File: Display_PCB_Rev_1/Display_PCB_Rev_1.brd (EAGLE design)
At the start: 5 parts, among them J1 71430-015

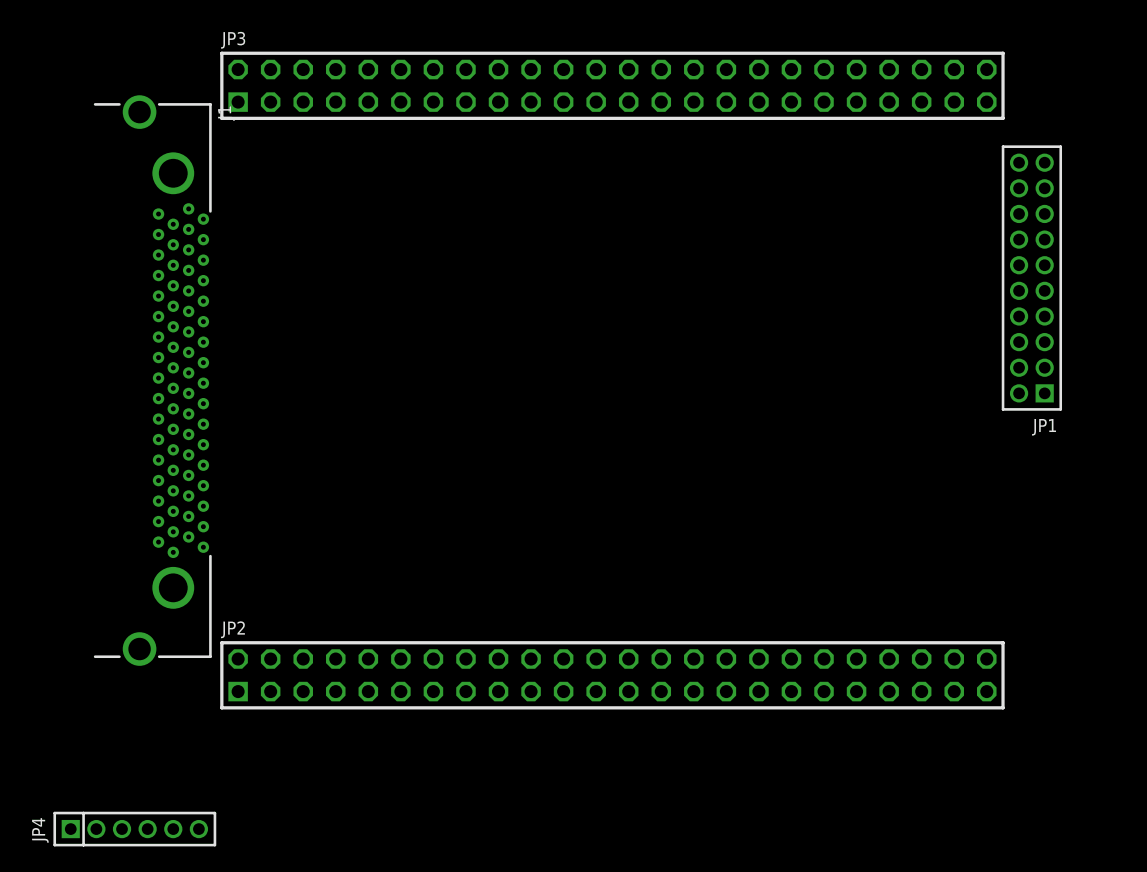
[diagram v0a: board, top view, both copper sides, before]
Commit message: Cleaned up schematic and layout; Added DC Barrel Jack and coupling capacitor; filtering circuit for shield
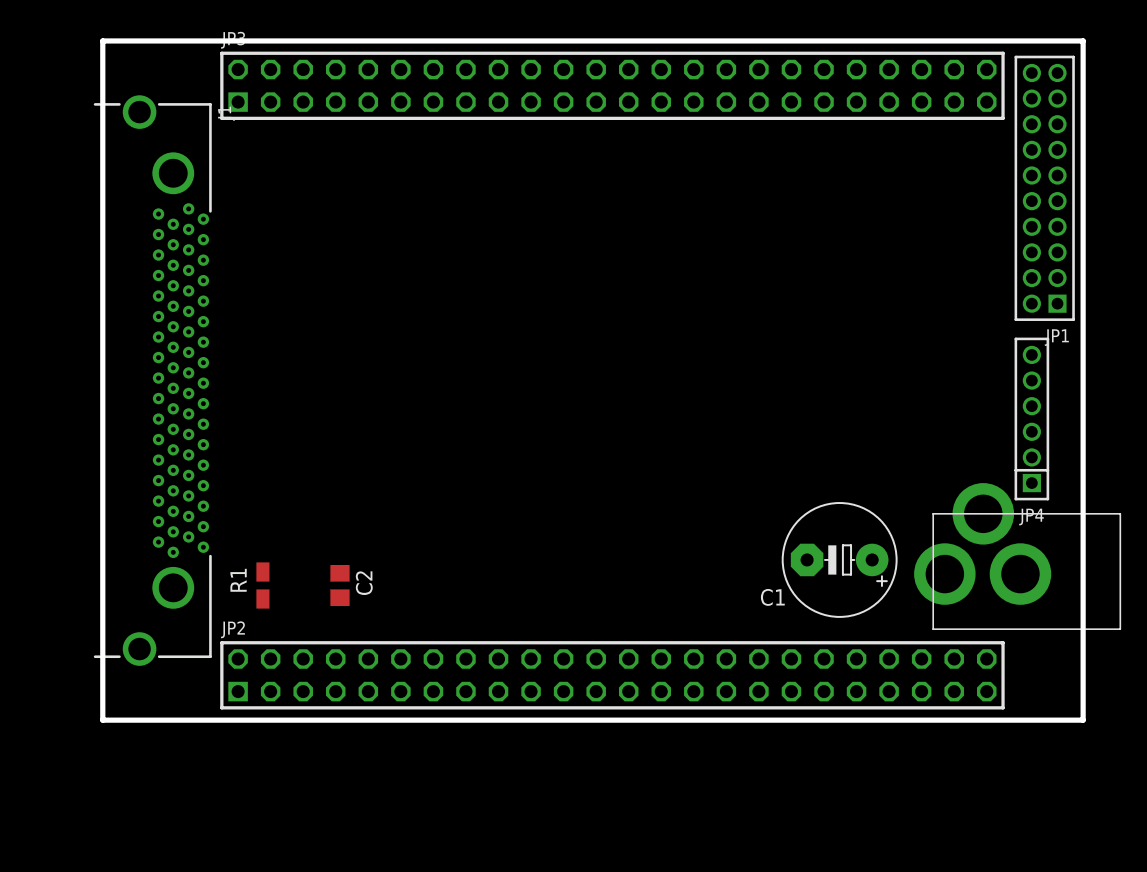
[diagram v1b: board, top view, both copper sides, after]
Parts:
- added C1: 220u, resistor:E5-8,5
- added C2: 1n, resistor:C0805
- added R1: 1M, resistor:R0805W
- added U$1: 2.1MMJACKTHM, adafruit:PJ-102A
- moved JP4 77.0 mm to (85.0, 51.0), turned to 90 degrees
- moved JP1 7.07 mm to (86.0, 69.0)
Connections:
- removed net N$2: JP3.25, JP3.41
- removed net N$4: J1.41
- new net DE: JP4.4
- new net VCC_12: C1.+, JP4.5, JP4.6, U$1.TIP
- net GND: now also C1.-, C2.2, JP2.1, JP2.11, JP2.12, JP2.17, JP2.2, JP2.26, JP2.33, JP2.42, JP3.16, JP3.23, JP3.32, JP3.39, JP3.48, JP3.7, JP4.1, JP4.2, R1.1, U$1.RING, U$1.RING_SW; no longer JP1.4, JP2.16, JP2.23, JP2.32, JP2.39, JP2.48, JP2.7, JP3.1, JP3.11, JP3.12, JP3.17, JP3.2, JP3.26, JP3.33, JP3.42
- net N$1: now also C2.1, R1.2; no longer JP3.18, JP3.34
- net VCC: now also J1.19, JP2.18, JP2.25, JP2.34, JP2.41, JP3.15, JP3.24, JP3.31, JP3.40, JP3.8; no longer JP1.3
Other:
- board outline added: 76.5 x 53 mm

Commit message: Added .gitignore; removed unnecessary files; added routes for VCC, GND, and VCC_12
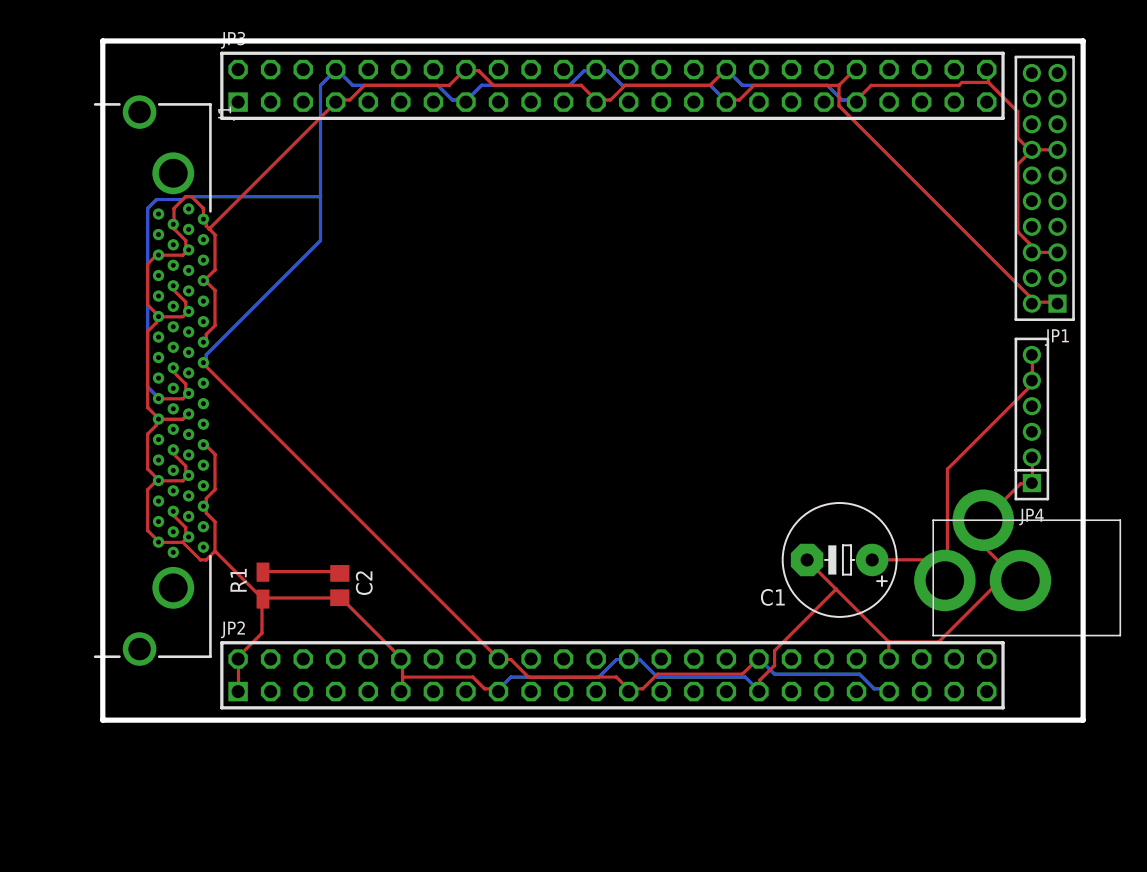
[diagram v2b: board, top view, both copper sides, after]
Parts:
- moved U$1 0.50 mm to (87.5, 38.5)
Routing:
- net GND: track 0.00 -> 274.4 mm
- net VCC: track 0.00 -> 198.1 mm
- net VCC_12: track 0.00 -> 28.1 mm
- net N$1: track 0.00 -> 6.06 mm

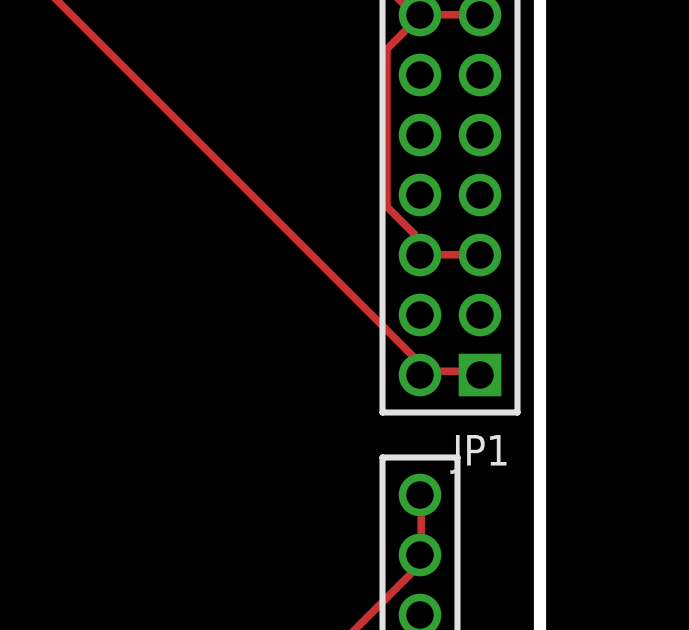
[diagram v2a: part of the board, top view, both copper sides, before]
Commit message: first set of differential pairs
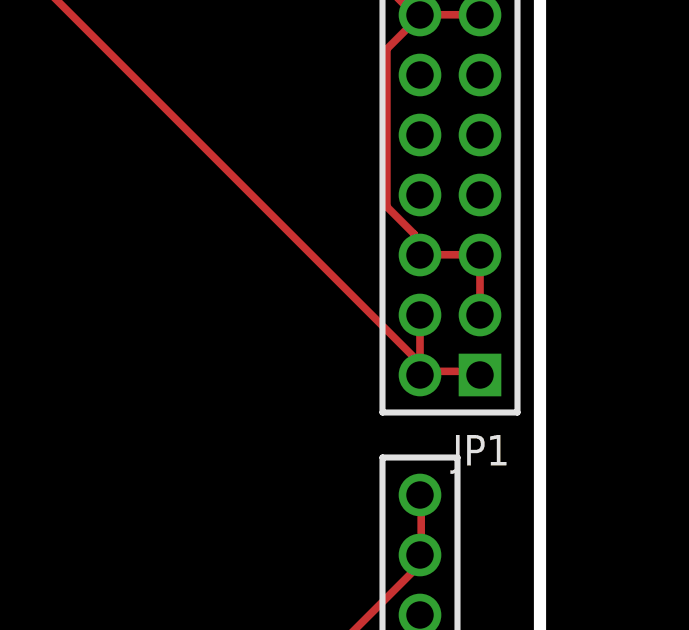
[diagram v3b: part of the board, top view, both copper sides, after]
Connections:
- net CLK_N: now also J1.66, JP3.12; no longer J1.9
- net CLK_P: now also J1.32, JP3.11; no longer J1.10
- net DE: now also J1.3, JP2.30
- net GND: now also JP1.3
- net RXIN0_N: now also J1.41, JP3.2; no longer J1.31
- net RXIN0_P: now also J1.7, JP3.1; no longer J1.32
- net RXIN1_N: now also J1.47, JP3.4; no longer J1.25
- net RXIN1_P: now also J1.13, JP3.3; no longer J1.26
- net RXIN2_N: now also J1.60, JP3.10; no longer J1.17
- net RXIN2_P: now also J1.26, JP3.9; no longer J1.18
- net VCC: now also JP1.4
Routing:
- net VCC: track 198.1 -> 200.1 mm
- net GND: track 274.4 -> 276.4 mm
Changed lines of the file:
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@@
 <wire x1="20.8026" y1="65.8368" x2="30.6324" y2="75.6666" width="0.254" layer="1"/>
 <wire x1="30.6324" y1="75.6666" x2="30.68" y2="75.73" width="0.254" layer="1"/>
-<wire x1="16.6878" y1="58.5216" x2="18" y2="56.595" width="0" layer="19" extent="1-1"/>
+<contactref element="JP1" pad="3"/>
+<wire x1="18" y1="56.595" x2="16.6878" y2="58.5216" width="0" layer="19" extent="1-1"/>
+<wire x1="87" y1="64" x2="87" y2="62" width="0.254" layer="1"/>
 </signal>
 <signal name="VCC">
@@
 <wire x1="50.9778" y1="78.1812" x2="51" y2="78.27" width="0.254" layer="16"/>
 <wire x1="40.9194" y1="75.8952" x2="40.84" y2="75.73" width="0.254" layer="16"/>
+<contactref element="JP1" pad="4"/>
+<wire x1="85" y1="62" x2="85" y2="60" width="0.254" layer="1"/>
 </signal>
 <signal name="RXIN0_N">
 <contactref element="JP1" pad="7"/>
-<contactref element="J1" pad="31"/>
-<wire x1="20.35" y1="64.995" x2="87" y2="66" width="0" layer="19" extent="1-1"/>
+<contactref element="J1" pad="41"/>
+<contactref element="JP3" pad="2"/>
+<wire x1="23.06" y1="78.27" x2="87" y2="66" width="0" layer="19" extent="1-1"/>
+<wire x1="18" y1="45.395" x2="23.06" y2="78.27" width="0" layer="19" extent="1-1"/>
 </signal>
 <signal name="RXIN1_N">
 <contactref element="JP1" pad="9"/>
-<contactref element="J1" pad="25"/>
-<wire x1="20.35" y1="60.195" x2="87" y2="68" width="0" layer="19" extent="1-1"/>
+<contactref element="J1" pad="47"/>
+<contactref element="JP3" pad="4"/>
+<wire x1="25.6" y1="78.27" x2="87" y2="68" width="0" layer="19" extent="1-1"/>
+<wire x1="18" y1="50.195" x2="25.6" y2="78.27" width="0" layer="19" extent="1-1"/>
 </signal>
 <signal name="RXIN0_P">
-<contactref element="J1" pad="32"/>
 <contactref element="JP1" pad="8"/>
-<wire x1="19.2" y1="65.795" x2="85" y2="66" width="0" layer="19" extent="1-1"/>
+<contactref element="J1" pad="7"/>
+<contactref element="JP3" pad="1"/>
+<wire x1="23.06" y1="75.73" x2="85" y2="66" width="0" layer="19" extent="1-1"/>
+<wire x1="20.35" y1="45.795" x2="23.06" y2="75.73" width="0" layer="19" extent="1-1"/>
 </signal>
 <signal name="RXIN1_P">
-<contactref element="J1" pad="26"/>
 <contactref element="JP1" pad="10"/>
-<wire x1="19.2" y1="60.995" x2="85" y2="68" width="0" layer="19" extent="1-1"/>
+<contactref element="J1" pad="13"/>
+<contactref element="JP3" pad="3"/>
+<wire x1="25.6" y1="75.73" x2="85" y2="68" width="0" layer="19" extent="1-1"/>
+<wire x1="20.35" y1="50.595" x2="25.6" y2="75.73" width="0" layer="19" extent="1-1"/>
 </signal>
 <signal name="RXIN2_N">
 <contactref element="JP1" pad="11"/>
-<contactref element="J1" pad="17"/>
-<wire x1="20.35" y1="53.795" x2="87" y2="70" width="0" layer="19" extent="1-1"/>
+<contactref element="J1" pad="60"/>
+<contactref element="JP3" pad="10"/>
+<wire x1="33.22" y1="78.27" x2="87" y2="70" width="0" layer="19" extent="1-1"/>
+<wire x1="16.85" y1="60.595" x2="33.22" y2="78.27" width="0" layer="19" extent="1-1"/>
 </signal>
 <signal name="RXIN2_P">
 <contactref element="JP1" pad="12"/>
-<contactref element="J1" pad="18"/>
-<wire x1="19.2" y1="54.595" x2="85" y2="70" width="0" layer="19" extent="1-1"/>
+<contactref element="J1" pad="26"/>
+<contactref element="JP3" pad="9"/>
+<wire x1="33.22" y1="75.73" x2="85" y2="70" width="0" layer="19" extent="1-1"/>
+<wire x1="19.2" y1="60.995" x2="33.22" y2="75.73" width="0" layer="19" extent="1-1"/>
 </signal>
 <signal name="CLK_N">
 <contactref element="JP1" pad="15"/>
-<contactref element="J1" pad="9"/>
-<wire x1="20.35" y1="47.395" x2="87" y2="74" width="0" layer="19" extent="1-1"/>
+<contactref element="J1" pad="66"/>
+<contactref element="JP3" pad="12"/>
+<wire x1="35.76" y1="78.27" x2="87" y2="74" width="0" layer="19" extent="1-1"/>
+<wire x1="16.85" y1="65.395" x2="35.76" y2="78.27" width="0" layer="19" extent="1-1"/>
 </signal>
 <signal name="CLK_P">
 <contactref element="JP1" pad="16"/>
-<contactref element="J1" pad="10"/>
-<wire x1="19.2" y1="48.195" x2="85" y2="74" width="0" layer="19" extent="1-1"/>
+<contactref element="J1" pad="32"/>
+<contactref element="JP3" pad="11"/>
+<wire x1="35.76" y1="75.73" x2="85" y2="74" width="0" layer="19" extent="1-1"/>
+<wire x1="19.2" y1="65.795" x2="35.76" y2="75.73" width="0" layer="19" extent="1-1"/>
 </signal>
 <signal name="VCC_12">
@@
 <signal name="DE">
 <contactref element="JP4" pad="4"/>
+<contactref element="J1" pad="3"/>
+<contactref element="JP2" pad="30"/>
+<wire x1="58.62" y1="32.27" x2="85" y2="52" width="0" layer="19" extent="1-1"/>
+<wire x1="20.35" y1="42.595" x2="58.62" y2="32.27" width="0" layer="19" extent="1-1"/>
 </signal>
 <signal name="N$1">

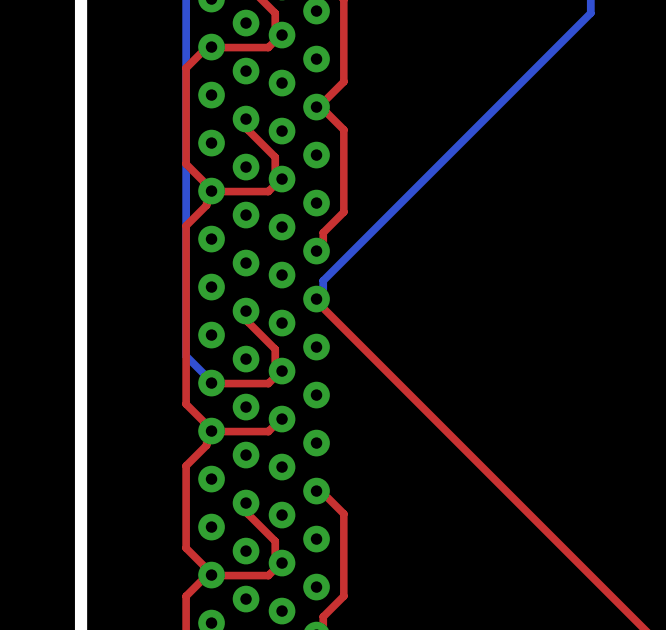
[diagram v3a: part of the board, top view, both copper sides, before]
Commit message: Starting the wiring of the VHDCI connections
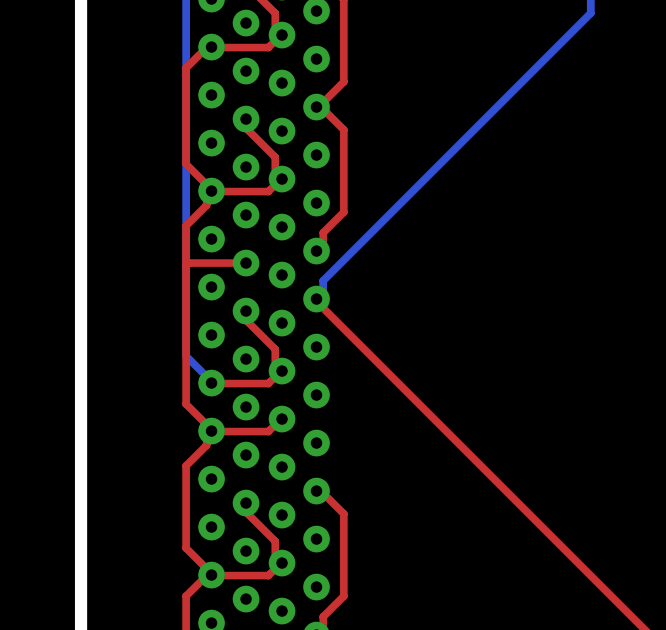
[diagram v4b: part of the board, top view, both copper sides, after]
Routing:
- net RXIN0_N: track 0.00 -> 97.9 mm
- net RXIN0_P: track 0.00 -> 67.5 mm
- net RXIN1_N: track 0.00 -> 42.2 mm
- net RXIN2_N: track 0.00 -> 35.3 mm
- net CLK_N: track 0.00 -> 21.0 mm
- net GND: track 276.4 -> 278.4 mm
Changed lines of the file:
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@@
 <wire x1="16.6878" y1="58.5216" x2="16.6878" y2="58.9788" width="0.254" layer="1"/>
 <wire x1="16.002" y1="57.8358" x2="16.6878" y2="58.5216" width="0.254" layer="1"/>
-<wire x1="16.002" y1="51.8922" x2="16.002" y2="57.8358" width="0.254" layer="1"/>
+<wire x1="16.002" y1="51.8922" x2="16.002" y2="56.5" width="0.254" layer="1"/>
+<wire x1="16.002" y1="56.5" x2="16.002" y2="57.8358" width="0.254" layer="1"/>
 <wire x1="16.6878" y1="51.2064" x2="16.002" y2="51.8922" width="0.254" layer="1"/>
 <wire x1="16.6878" y1="58.9788" x2="16.85" y2="58.995" width="0.254" layer="1"/>
@@
 <wire x1="30.6324" y1="75.6666" x2="30.68" y2="75.73" width="0.254" layer="1"/>
 <contactref element="JP1" pad="3"/>
-<wire x1="18" y1="56.595" x2="16.6878" y2="58.5216" width="0" layer="19" extent="1-1"/>
 <wire x1="87" y1="64" x2="87" y2="62" width="0.254" layer="1"/>
+<wire x1="18" y1="56.595" x2="16.097" y2="56.595" width="0.254" layer="1"/>
+<wire x1="16.097" y1="56.595" x2="16.002" y2="56.5" width="0.254" layer="1"/>
 </signal>
 <signal name="VCC">
@@
 <contactref element="J1" pad="41"/>
 <contactref element="JP3" pad="2"/>
-<wire x1="23.06" y1="78.27" x2="87" y2="66" width="0" layer="19" extent="1-1"/>
-<wire x1="18" y1="45.395" x2="23.06" y2="78.27" width="0" layer="19" extent="1-1"/>
+<wire x1="87" y1="66" x2="86" y2="65" width="0.254" layer="2"/>
+<wire x1="86" y1="65" x2="83.5" y2="65" width="0.254" layer="2"/>
+<wire x1="83.5" y1="65" x2="82.679284375" y2="64.355996875" width="0.254" layer="2"/>
+<wire x1="82.679284375" y1="64.355996875" x2="80.16164375" y2="61.83835625" width="0.254" layer="2"/>
+<wire x1="80.161646875" y1="61.838353125" x2="63.59469375" y2="45.2714" width="0.254" layer="2"/>
+<wire x1="63.59469375" y1="45.2714" x2="26" y2="45.2714" width="0.254" layer="2"/>
+<wire x1="19.7640125" y1="45.471975" x2="19.706340625" y2="45.58731875" width="0" layer="19" extent="1-16"/>
+<wire x1="19.706340625" y1="45.58731875" x2="18.0721" y2="45.8274125" width="0" layer="19" curve="85.401073" extent="1-16"/>
+<wire x1="18.0721" y1="45.8274125" x2="18" y2="45.395" width="0" layer="19" extent="1-16"/>
+<wire x1="19.861803125" y1="44.72360625" x2="19.816228125" y2="44.63245625" width="0" layer="19" extent="1-16"/>
+<wire x1="19.816228125" y1="44.63245625" x2="18.86754375" y2="44.316228125" width="0" layer="19" curve="-90" extent="1-16"/>
+<wire x1="18.86754375" y1="44.316228125" x2="18.5" y2="44.5" width="0" layer="19" extent="1-16"/>
+<wire x1="80.161646875" y1="61.838353125" x2="80.16164375" y2="61.83835625" width="0" layer="19" extent="2-2"/>
+<wire x1="23.06" y1="78.27" x2="80.16164375" y2="61.83835625" width="0" layer="19" extent="1-2"/>
+<wire x1="26" y1="45.2714" x2="22" y2="39.5" width="0" layer="19" extent="1-16"/>
+<wire x1="22" y1="39.5" x2="18" y2="45.395" width="0" layer="19" extent="1-16"/>
+<wire x1="18" y1="45.395" x2="15.5" y2="45.395" width="0.254" layer="2"/>
+<wire x1="15.5" y1="45.395" x2="15.5" y2="35.5" width="0.254" layer="2"/>
+<wire x1="15.5" y1="35.5" x2="22" y2="35.5" width="0.254" layer="2"/>
+<wire x1="22" y1="35.5" x2="22" y2="45" width="0.254" layer="2"/>
+<wire x1="22" y1="45" x2="26" y2="45.2714" width="0" layer="19" extent="1-16"/>
 </signal>
 <signal name="RXIN1_N">
@@
 <contactref element="JP3" pad="4"/>
 <wire x1="25.6" y1="78.27" x2="87" y2="68" width="0" layer="19" extent="1-1"/>
-<wire x1="18" y1="50.195" x2="25.6" y2="78.27" width="0" layer="19" extent="1-1"/>
+<wire x1="18" y1="50.195" x2="14.5" y2="50.195" width="0.254" layer="2"/>
+<wire x1="14.5" y1="50.195" x2="14.5" y2="35" width="0.254" layer="2"/>
+<wire x1="14.5" y1="35" x2="23" y2="35" width="0.254" layer="2"/>
+<wire x1="23" y1="35" x2="23" y2="50" width="0.254" layer="2"/>
+<wire x1="23" y1="50" x2="25.6" y2="78.27" width="0" layer="19" extent="1-16"/>
 </signal>
 <signal name="RXIN0_P">
@@
 <contactref element="J1" pad="7"/>
 <contactref element="JP3" pad="1"/>
-<wire x1="23.06" y1="75.73" x2="85" y2="66" width="0" layer="19" extent="1-1"/>
-<wire x1="20.35" y1="45.795" x2="23.06" y2="75.73" width="0" layer="19" extent="1-1"/>
+<wire x1="85" y1="66" x2="83.5" y2="66" width="0.254" layer="2"/>
+<wire x1="83.5" y1="66" x2="82.350628125" y2="64.673915625" width="0.254" layer="2"/>
+<wire x1="82.350628125" y1="64.673915625" x2="79.83835625" y2="62.16164375" width="0.254" layer="2"/>
+<wire x1="79.838353125" y1="62.161646875" x2="63.40530625" y2="45.7286" width="0.254" layer="2"/>
+<wire x1="63.40530625" y1="45.7286" x2="26" y2="45.7286" width="0.254" layer="2"/>
+<wire x1="26" y1="45.7286" x2="20.9336" y2="45.795" width="0" layer="19" extent="1-16"/>
+<wire x1="20.9336" y1="45.795" x2="20.35" y2="45.795" width="0" layer="19" extent="1-16"/>
+<wire x1="79.838353125" y1="62.161646875" x2="79.83835625" y2="62.16164375" width="0" layer="19" extent="2-2"/>
+<wire x1="23.06" y1="75.73" x2="79.83835625" y2="62.16164375" width="0" layer="19" extent="1-2"/>
 </signal>
 <signal name="RXIN1_P">
@@
 <contactref element="JP3" pad="10"/>
 <wire x1="33.22" y1="78.27" x2="87" y2="70" width="0" layer="19" extent="1-1"/>
-<wire x1="16.85" y1="60.595" x2="33.22" y2="78.27" width="0" layer="19" extent="1-1"/>
+<wire x1="16.85" y1="60.595" x2="14.5" y2="60.595" width="0.254" layer="2"/>
+<wire x1="14.5" y1="60.595" x2="14.5" y2="73" width="0.254" layer="2"/>
+<wire x1="14.5" y1="73" x2="23.5" y2="73" width="0.254" layer="2"/>
+<wire x1="23.5" y1="73" x2="23.5" y2="61.5" width="0.254" layer="2"/>
+<wire x1="23.5" y1="61.5" x2="33.22" y2="78.27" width="0" layer="19" extent="1-16"/>
 </signal>
 <signal name="RXIN2_P">
@@
 <contactref element="JP3" pad="12"/>
 <wire x1="35.76" y1="78.27" x2="87" y2="74" width="0" layer="19" extent="1-1"/>
-<wire x1="16.85" y1="65.395" x2="35.76" y2="78.27" width="0" layer="19" extent="1-1"/>
+<wire x1="16.85" y1="65.395" x2="15.5" y2="65.395" width="0.254" layer="2"/>
+<wire x1="15.5" y1="65.395" x2="15.5" y2="72.5" width="0.254" layer="2"/>
+<wire x1="15.5" y1="72.5" x2="22.5" y2="72.5" width="0.254" layer="2"/>
+<wire x1="22.5" y1="72.5" x2="22.5" y2="67" width="0.254" layer="2"/>
+<wire x1="22.5" y1="67" x2="35.76" y2="78.27" width="0" layer="19" extent="1-16"/>
 </signal>
 <signal name="CLK_P">
